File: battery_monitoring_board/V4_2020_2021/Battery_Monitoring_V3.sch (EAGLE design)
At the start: 93 parts, among them CON1 MOLEX_5566-2, CON2 SM03B-GHS-TB, CON3 SM03B-GHS-TB, J1 MKDS_5/2-6,352, J10 MKDS_5/2-6,352, J11 MKDS_5/2-6,352, J2 MKDS_5/2-6,352, J3 MKDS_5/2-6,352, J4 MKDS_5/2-6,352, J5 MKDS_5/2-6,352, J6 MKDS_5/2-6,352, J7 MKDS_5/2-6,352, J8 MKDS_5/2-6,352, J9 MKDS_5/2-6,352, Q1 TCLD1000CT, Q10 SI7145DP, Q11 SI7145DP, Q12 SI7145DP, Q13 SI7145DP, Q14 SI7145DP, Q15 PSMN1R5-30BLE, Q16 TCLD1000CT, Q2 TCLD1000CT, Q3 TCLD1000CT, Q4 PSMN1R5-30BLE, Q5 PSMN1R5-30BLE, Q6 PSMN1R5-30BLE, Q7 SI7145DP, Q8 SI7145DP, Q9 SI7145DP, U1 INA3221., U2 INA3221., U3 TEENSY_3.1_BASIC_2, U4 TCAN1042HVDR, U5 LTC4418

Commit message: started new sheet
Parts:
- added 3V3, DANGER: (no value), adafruit:LEDSMT1206
- added C13, C14, C15, C16: 0.01uF, adafruit:C-USC0805
- added C17: 10uF, adafruit:C-USC1206
- added C18: 1.5uF, adafruit:C-USC0805
- added CON4: MOLEX_5566-2, ARVP:MOLEX_5566-2
- added D5: (no value), diode:DIODE-DO-214AC
- added J12, J13, J14, J15, J16, J17: MKDS_5/2-6,352, Moira:MKDS_5/2-6,352
- added JP7: (no value), pinhead:PINHD-1X2
- added Q17, Q18, Q19, Q20: NMOS-TO252, AlbertaSat:NMOS-TO252
- added Q21: DMN2011UTS, Lydia:DMN2011UTS
- added R39, R40: 240, resistor:R-US_R1206
- added R41, R42, R43, R44: 100k, adafruit:R-US_R1206
- added R45: 5.1, adafruit:R-US_R1206
- added R46: 1k, rcl:R-US_R0805
- added U10, U6, U7, U8: LM5050-2, AlbertaSat:LM5050-2
- added U12: IR2301S, Lydia:IR2301S
- added U9: TEENSY_3.1_BASIC_2, Teensy_3_Series_Board_v1.0:TEENSY_3.1_BASIC_2
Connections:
- new net +5V1: JP7.2
- new net GATE1: Q17.G, U6.GATE
- new net GATE2: Q18.G, U7.GATE
- new net GATE3: Q19.G, U8.GATE
- new net GATE4: Q20.G, U10.GATE
- new net GATE5: R46.1, U12.HO
- new net IO1: U12.HIN, U9.10/TX2/PWM
- new net IO2: U10.OFF, U6.OFF, U7.OFF, U8.OFF, U9.6/PWM
- new net IO3: R42.1, U7.NFGD, U9.8/TX3
- new net IO4: R41.1, U8.NFGD, U9.5/PWM
- new net IO5: R43.1, U6.NFGD, U9.9/RX2/PWM
- new net IO6: R44.1, U10.NFGD, U9.7/RX3
- new net LEAK_IN: U9.14/A0
- new net LED_D: R39.1, U9.23/A9/T/PWM
- new net N$12: DANGER.A, R39.2
- new net N$13: C17.1, J15.KL1, Q21.D, R45.1, U12.VCC
- new net N$17: 3V3.A, R40.1
- new net N$18: C18.2, U12.VS
- new net N$19: C18.1, D5.C, U12.VB
- new net N$20: Q21.G, R46.2
- new net N$21: D5.A, R45.2
- new net VBATT1: C14.1, J14.KL1, Q17.S, U6.IN
- new net VBATT2: C13.1, J13.KL1, Q18.S, U7.IN
- new net VBATT3: C15.1, J12.KL1, Q19.S, U8.IN
- new net VBATT4: C16.1, J17.KL1, Q20.S, U10.IN
- new net VIN1: JP7.1
- new net VOUT: J16.KL, Q17.D, Q18.D, Q19.D, Q20.D, Q21.S, U10.OUT, U6.OUT, U7.OUT, U8.OUT
- net +3V3: now also R40.2, U9.3.3V
- net +5V: now also CON4G$1.S, R41.2, R42.2, R43.2, R44.2
- net GND: now also 3V3.C, C13.2, C14.2, C15.2, C16.2, C17.2, CON4G$2.S, DANGER.C, J12.KL, J13.KL, J14.KL, J15.KL, J16.KL1, J17.KL, U10.GND, U12.GND, U12.LIN, U6.GND, U7.GND, U8.GND, U9.GND
- net VIN: now also U9.VIN
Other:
- note added: "5V into Teensy"
- note added: "A high side NMOS switch controls the original electronics battery (BATT0) using a high side gate driver with a bootstap circuit. When the GPIO pin is low, the NMOS is not conducting. When the GPIO pin is high, the gate driver will turn on and drive the NMOS with battery voltage+bootstrap voltage."
- note added: "IO1 is an output and controls the electronic battery BATT0. IO2 is an output and controls all the LM5050s. IO3, 4, 5 are inputs and sense the state of the NMOS on LM5050 (see if they are shorted)."
- note added: "Oring Config"
- note added: "Teensy and CAN bus"
- note added: "The LM5050MK-2 ideal diode OR control compare the voltages of the 3 motor batteries (BATT1 to BATT3) and use the one with the higher voltage to supply the electronics to achieve battery balancing. BATT0 should not be in use when the LM5050s are in use. The OFF pin on the LM5050 act like a switch, when it is high the NMOS gate is off. (Although the primary use of OFF is to test whether the FET is 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"
- note added: "The bootstrap circuit uses a capacitor C7 to store charge on a low cycle. Stored charge will be used to bias VCC to increase the voltage at HO during high cycles in order to increase the voltage between the NMOS gate and source. C7 will slowly discharge during a high cycle, so the capcitance is chosen to be 10 times greater than the gate capacitance of the NMOS to prolong the discharge. The bypas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"
- note added: "The teensy controls the switching between BATT0 and BATT1-3. It also includes the CAN bus and LED signals."
- note added: "The wall power terminal & the electronics battery pass through the hotswap IC(sheet 2) before going to the INA then out the terminal to the power board. This rail does not need to turn off with the kill switch and receives reverse voltage protection from the hotswap IC."
- note removed: "The wall power terminal & the electronics battery pass through the hotswap IC(sheet 2) before going to the INA then out the terminal to the power boar. This rail does not need to turn off with the kill switch and receives reverse voltage protection from the hotswap IC."

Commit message: Removed duplicate teensy
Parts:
- removed 3V3, DANGER: (no value), adafruit:LEDSMT1206
- removed CON4: MOLEX_5566-2, ARVP:MOLEX_5566-2
- removed JP7: (no value), pinhead:PINHD-1X2
- removed R39, R40: 240, resistor:R-US_R1206
- removed U9: TEENSY_3.1_BASIC_2, Teensy_3_Series_Board_v1.0:TEENSY_3.1_BASIC_2
- added 3V1, DANGER1: (no value), adafruit:LEDSMT1206
- added R36, R37: 240, resistor:R-US_R1206
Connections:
- removed net +5V1: JP7.2
- removed net N$12: DANGER.A, R39.2
- removed net N$17: 3V3.A, R40.1
- removed net VIN1: JP7.1
- new net N$22: 3V1.A, R37.1
- new net N$23: DANGER1.A, R36.2
- net +3V3: now also R37.2; no longer R40.2, U9.3.3V
- net +5V: no longer CON4G$1.S
- net GND: now also 3V1.C, DANGER1.C; no longer 3V3.C, CON4G$2.S, DANGER.C, U9.GND
- net IO1: now also U3.17/A3/T; no longer U9.10/TX2/PWM
- net IO2: now also U3.13/SCK/LED; no longer U9.6/PWM
- net IO3: now also U3.15/A1/T; no longer U9.8/TX3
- net IO4: now also U3.12/MISO; no longer U9.5/PWM
- net IO5: now also U3.16/A2/T; no longer U9.9/RX2/PWM
- net IO6: now also U3.14/A0; no longer U9.7/RX3
- net LEAK_IN: now also U3.11/MOSI; no longer U9.14/A0
- net LED_D: now also R36.1, U3.23/A9/T/PWM; no longer R39.1, U9.23/A9/T/PWM
- net VIN: no longer U9.VIN

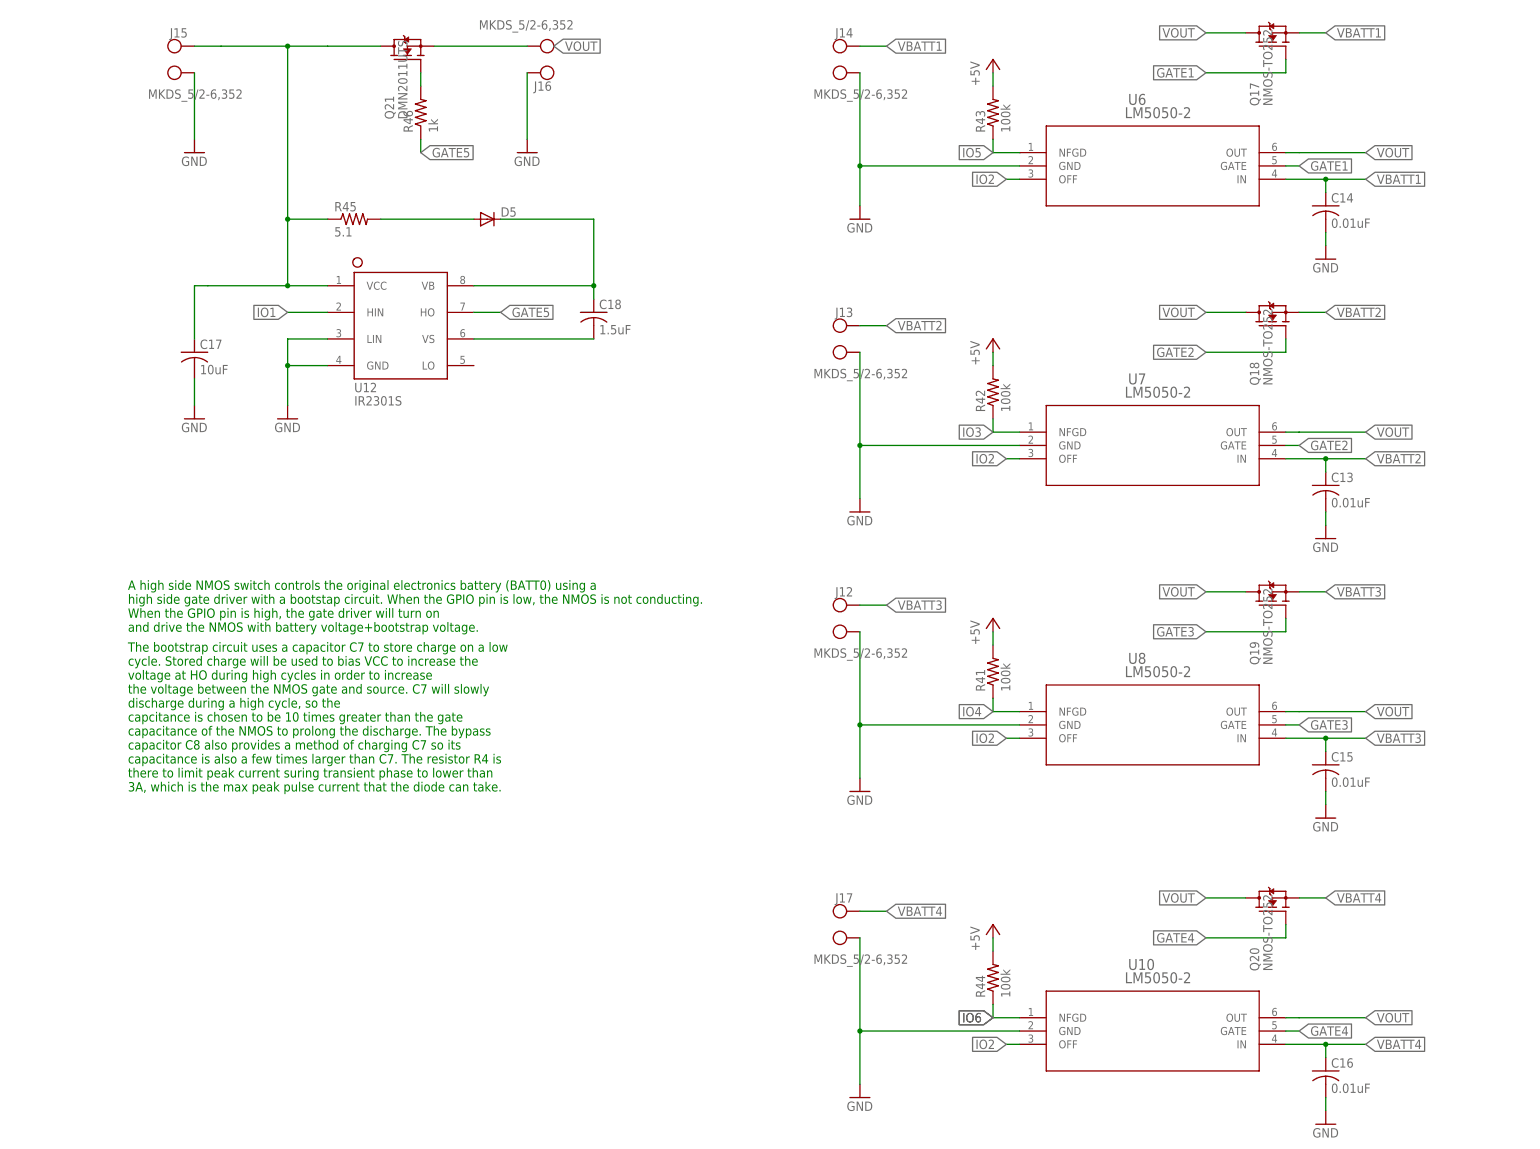
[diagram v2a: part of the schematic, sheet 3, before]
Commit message: Removed jumpers
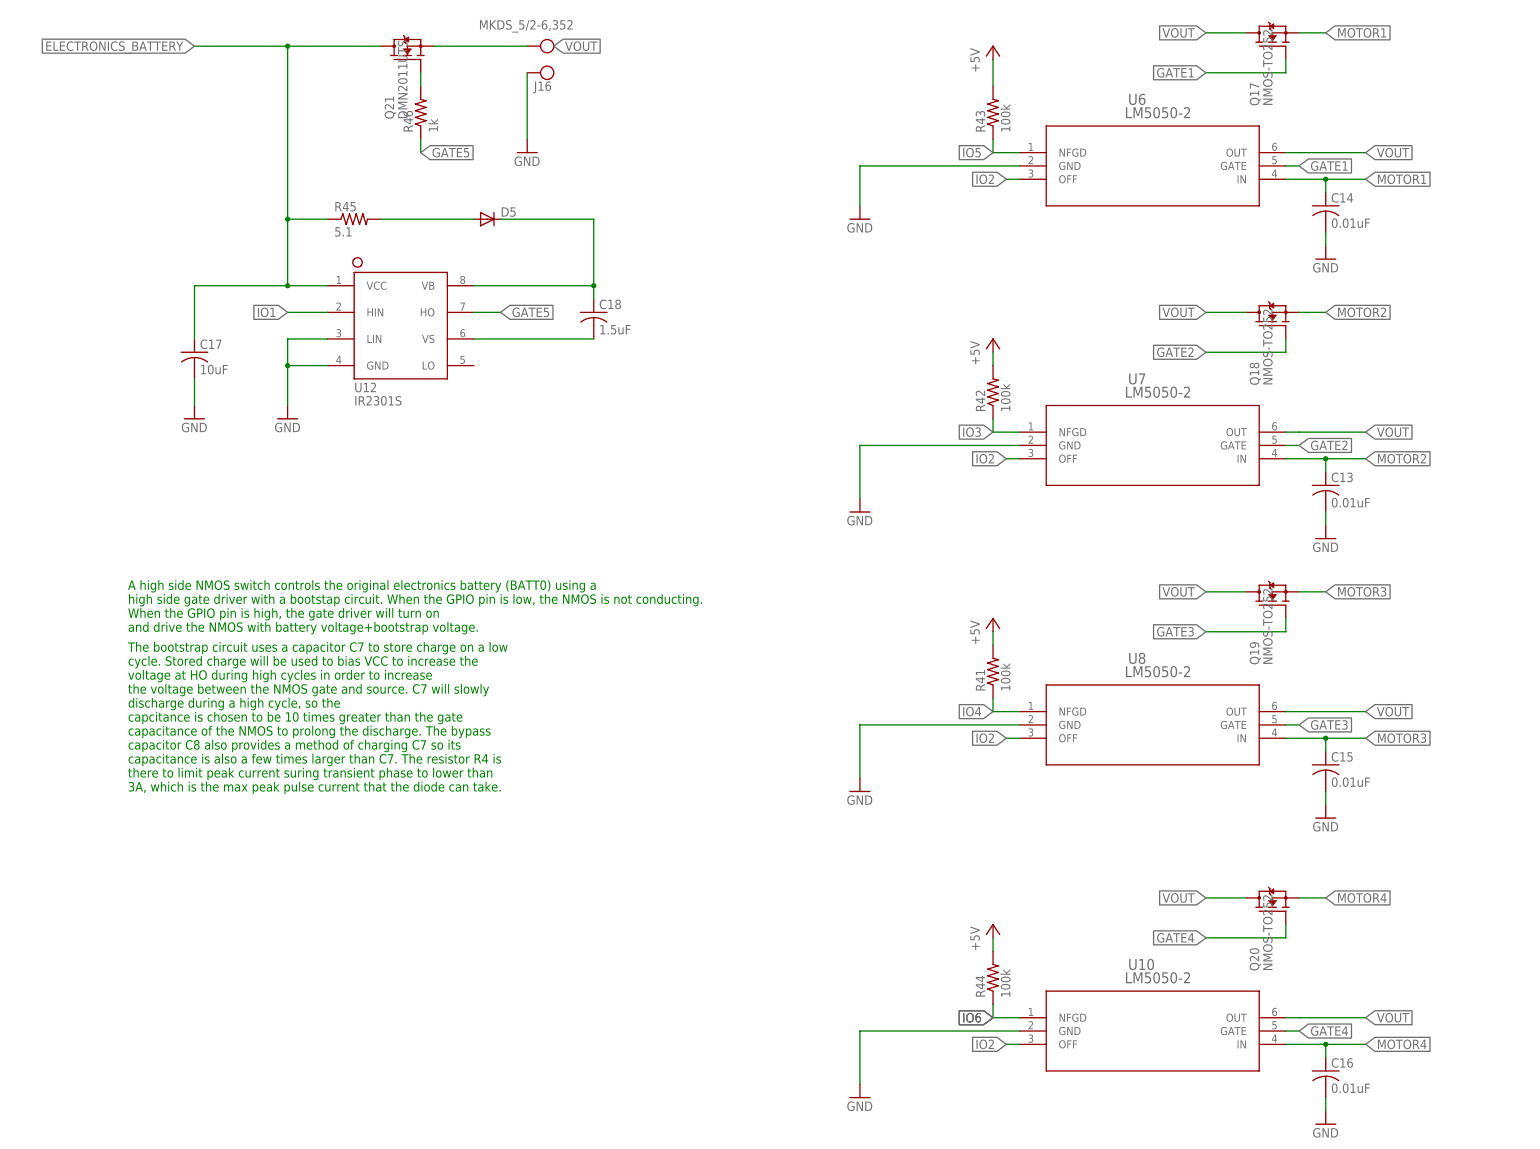
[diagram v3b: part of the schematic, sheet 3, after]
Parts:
- removed J11, J12, J13, J14, J15, J17, J5, J6, J7, J8: MKDS_5/2-6,352, Moira:MKDS_5/2-6,352
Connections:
- removed net LEAK_IN: U3.11/MOSI
- removed net N$13: C17.1, J15.KL1, Q21.D, R45.1, U12.VCC
- removed net VBATT1: C14.1, J14.KL1, Q17.S, U6.IN
- removed net VBATT2: C13.1, J13.KL1, Q18.S, U7.IN
- removed net VBATT3: C15.1, J12.KL1, Q19.S, U8.IN
- removed net VBATT4: C16.1, J17.KL1, Q20.S, U10.IN
- net ELECTRONICS_BATTERY: now also C17.1, Q21.D, R45.1, U12.VCC
- net GND: no longer J11.KL1, J12.KL, J13.KL, J14.KL, J15.KL, J17.KL, J5.KL1, J6.KL1, J7.KL1, J8.KL1
- net MOTOR1: now also C14.1, Q17.S, U6.IN; no longer J5.KL
- net MOTOR2: now also C13.1, Q18.S, U7.IN; no longer J6.KL
- net MOTOR3: now also C15.1, Q19.S, U8.IN; no longer J7.KL
- net MOTOR4: now also C16.1, Q20.S, U10.IN; no longer J11.KL
- net POWER_BOARD: no longer J8.KL
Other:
- note removed: "Motor Terminals"
- note removed: "OUTPUTS"

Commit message: started work on PCB layout
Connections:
- net ELECTRONICS_BATTERY: no longer C17.1, Q21.D, R45.1, U12.VCC
- net POWER_BOARD: now also C17.1, Q21.D, R45.1, U12.VCC
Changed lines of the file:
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@@
-</segment>
-</net>
-<net name="ELECTRONICS_BATTERY" class="0">
-<segment>
-<wire x1="-251.46" y1="63.5" x2="-233.68" y2="63.5" width="0.1524" layer="91"/>
-<wire x1="-233.68" y1="63.5" x2="-215.9" y2="63.5" width="0.1524" layer="91"/>
-<pinref part="Q21" gate="G$1" pin="D"/>
-<wire x1="-251.46" y1="7.62" x2="-251.46" y2="17.78" width="0.1524" layer="91"/>
-<pinref part="U12" gate="G$1" pin="VCC"/>
-<wire x1="-251.46" y1="17.78" x2="-233.68" y2="17.78" width="0.1524" layer="91"/>
-<wire x1="-233.68" y1="17.78" x2="-226.06" y2="17.78" width="0.1524" layer="91"/>
-<wire x1="-233.68" y1="63.5" x2="-233.68" y2="30.48" width="0.1524" layer="91"/>
-<junction x="-233.68" y="63.5"/>
-<junction x="-233.68" y="17.78"/>
-<pinref part="C17" gate="G$1" pin="1"/>
-<pinref part="R45" gate="G$1" pin="1"/>
-<wire x1="-233.68" y1="30.48" x2="-233.68" y2="17.78" width="0.1524" layer="91"/>
-<wire x1="-233.68" y1="30.48" x2="-226.06" y2="30.48" width="0.1524" layer="91"/>
-<junction x="-233.68" y="30.48"/>
-<label x="-251.46" y="63.5" size="1.778" layer="95" rot="R180" xref="yes"/>
 </segment>
 </net>
@@
 </segment>
 </net>
+<net name="POWER_BOARD" class="0">
+<segment>
+<pinref part="C17" gate="G$1" pin="1"/>
+<pinref part="U12" gate="G$1" pin="VCC"/>
+<wire x1="-251.46" y1="7.62" x2="-251.46" y2="17.78" width="0.1524" layer="91"/>
+<wire x1="-251.46" y1="17.78" x2="-233.68" y2="17.78" width="0.1524" layer="91"/>
+<wire x1="-226.06" y1="17.78" x2="-233.68" y2="17.78" width="0.1524" layer="91"/>
+<pinref part="R45" gate="G$1" pin="1"/>
+<wire x1="-233.68" y1="17.78" x2="-233.68" y2="30.48" width="0.1524" layer="91"/>
+<wire x1="-226.06" y1="30.48" x2="-233.68" y2="30.48" width="0.1524" layer="91"/>
+<pinref part="Q21" gate="G$1" pin="D"/>
+<wire x1="-233.68" y1="30.48" x2="-233.68" y2="63.5" width="0.1524" layer="91"/>
+<wire x1="-233.68" y1="63.5" x2="-215.9" y2="63.5" width="0.1524" layer="91"/>
+<wire x1="-215.9" y1="63.5" x2="-233.68" y2="63.5" width="0.1524" layer="91"/>
+<label x="-241.3" y="63.5" size="1.778" layer="95" rot="R180" xref="yes"/>
+<junction x="-233.68" y="63.5"/>
+<wire x1="-233.68" y1="63.5" x2="-241.3" y2="63.5" width="0.1524" layer="91"/>
+<junction x="-233.68" y="30.48"/>
+<junction x="-233.68" y="17.78"/>
+</segment>
+</net>
